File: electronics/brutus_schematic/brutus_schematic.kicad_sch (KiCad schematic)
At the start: 5 parts, among them U1 PCA9685PW, U2 ESP32 DevKit

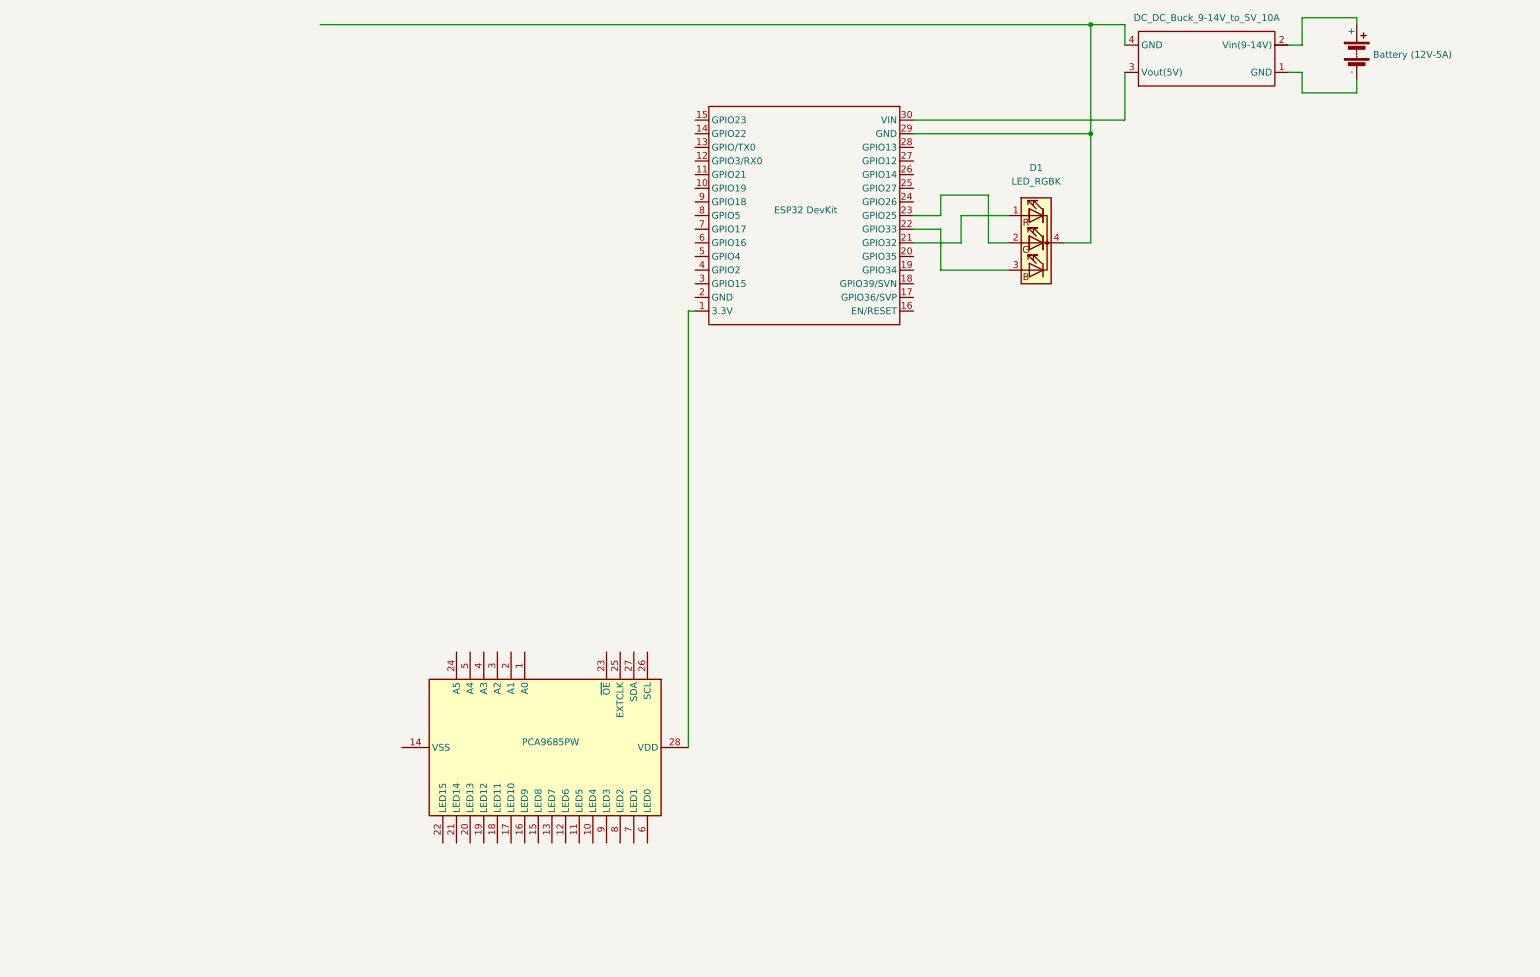
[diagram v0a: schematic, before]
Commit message: Added and connected servos, added and connected ultrasonic sensors, changed LED RGB GND pin
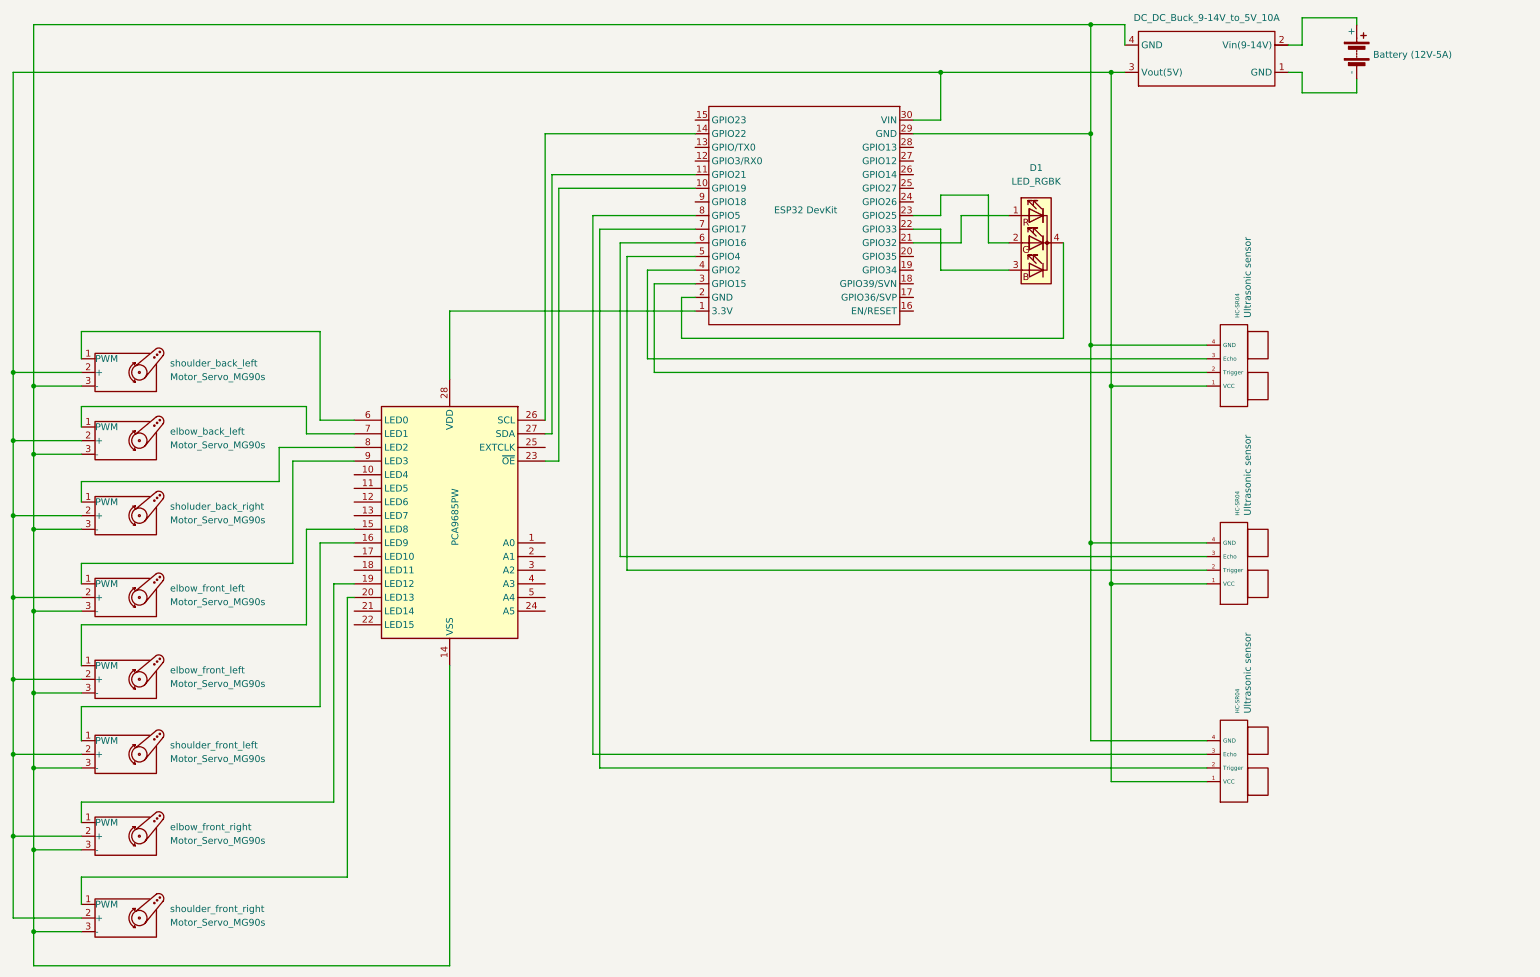
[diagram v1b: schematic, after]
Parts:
- added HC-SR04 (x3): Ultrasonic sensor, symbol hc-sr04:hc-sr04
- added elbow_back_left, elbow_front_left (x2), elbow_front_right, sholuder_back_right, shoulder_back_left, shoulder_front_left, shoulder_front_right: Motor_Servo_MG90s, symbol Motor:Motor_Servo
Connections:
- net at U1.14 (VSS): now also DCB.4 (GND), U2.29 (GND), HC-SR04.4 (GND), HC-SR04.4 (GND), HC-SR04.4 (GND), elbow_back_left.3 (-), elbow_front_left.3 (-), elbow_front_left.3 (-), elbow_front_right.3 (-), sholuder_back_right.3 (-), shoulder_back_left.3 (-), shoulder_front_left.3 (-), shoulder_front_right.3 (-)
- net at U1.15 (LED8): now also elbow_front_left.1 (PWM)
- net at U1.16 (LED9): now also shoulder_front_left.1 (PWM)
- net at U1.19 (LED12): now also elbow_front_right.1 (PWM)
- net at U1.20 (LED13): now also shoulder_front_right.1 (PWM)
- net at U1.23 (~{OE}): now also U2.10 (GPIO19)
- net at U1.26 (SCL): now also U2.14 (GPIO22)
- net at U1.27 (SDA): now also U2.11 (GPIO21)
- net at U1.6 (LED0): now also shoulder_back_left.1 (PWM)
- net at U1.7 (LED1): now also elbow_back_left.1 (PWM)
- net at U1.8 (LED2): now also sholuder_back_right.1 (PWM)
- net at U1.9 (LED3): now also elbow_front_left.1 (PWM)
- net at DCB.3 (Vout(5V)), U2.30 (VIN): now also HC-SR04.1 (VCC), HC-SR04.1 (VCC), HC-SR04.1 (VCC), elbow_back_left.2 (+), elbow_front_left.2 (+), elbow_front_left.2 (+), elbow_front_right.2 (+), sholuder_back_right.2 (+), shoulder_back_left.2 (+), shoulder_front_left.2 (+), shoulder_front_right.2 (+)
- net at U2.2 (GND): now also D1.4 (K)
- net at U2.3 (GPIO15): now also HC-SR04.2 (Trigger)
- net at U2.4 (GPIO2): now also HC-SR04.3 (Echo)
- net at U2.5 (GPIO4): now also HC-SR04.2 (Trigger)
- net at U2.6 (GPIO16): now also HC-SR04.3 (Echo)
- net at U2.7 (GPIO17): now also HC-SR04.2 (Trigger)
- net at U2.8 (GPIO5): now also HC-SR04.3 (Echo)

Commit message: adding switch to kiCad
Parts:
- added SWITCH: SW1, Button_Switch_SMD:Nidec_Copal_CAS-120A, symbol Switch:SW_Nidec_CAS-120A1
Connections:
- net at BT.2 (-): now also SWITCH.2 (B); no longer DCB.1 (GND)
- new net: DCB.1 (GND), SWITCH.3 (A)
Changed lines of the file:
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@@
+	)
+	(junction
+		(at 273.05 27.94)
+		(diameter 0)
+		(color 0 0 0 0)
 	)
 	(junction
@@
 	(wire
 		(pts
-			(xy 254 15.24) (xy 264.16 15.24)
+			(xy 254 15.24) (xy 273.05 15.24)
 		)
 		(stroke
@@
 	(wire
 		(pts
+			(xy 254 25.4) (xy 254 26.67)
+		)
+		(stroke
+			(width 0)
+			(type default)
+		)
+	)
+	(wire
+		(pts
 			(xy 199.39 57.15) (xy 195.58 57.15)
 		)
@@
 	(wire
 		(pts
-			(xy 264.16 26.67) (xy 264.16 29.21)
-		)
-		(stroke
-			(width 0)
-			(type default)
-		)
-	)
-	(wire
-		(pts
 			(xy 218.44 157.48) (xy 218.44 120.65)
 		)
@@
 	(wire
 		(pts
+			(xy 254 26.67) (xy 257.81 26.67)
+		)
+		(stroke
+			(width 0)
+			(type default)
+		)
+	)
+	(wire
+		(pts
 			(xy 17.78 154.94) (xy 26.67 154.94)
 		)
@@
 	(wire
 		(pts
-			(xy 264.16 15.24) (xy 264.16 16.51)
+			(xy 273.05 15.24) (xy 273.05 17.78)
 		)
 		(stroke
@@
 	(wire
 		(pts
-			(xy 254 25.4) (xy 254 29.21)
-		)
-		(stroke
-			(width 0)
-			(type default)
-		)
-	)
-	(wire
-		(pts
 			(xy 121.92 52.07) (xy 140.97 52.07)
 		)
@@
 	(wire
 		(pts
-			(xy 254 29.21) (xy 264.16 29.21)
-		)
-		(stroke
-			(width 0)
-			(type default)
-		)
-	)
-	(wire
-		(pts
 			(xy 114.3 92.71) (xy 114.3 44.45)
 		)
@@
 	(wire
 		(pts
+			(xy 273.05 26.67) (xy 273.05 27.94)
+		)
+		(stroke
+			(width 0)
+			(type default)
+		)
+	)
+	(wire
+		(pts
 			(xy 236.22 115.57) (xy 127 115.57)
 		)
@@
 	(wire
 		(pts
+			(xy 251.46 25.4) (xy 254 25.4)
+		)
+		(stroke
+			(width 0)
+			(type default)
+		)
+	)
+	(wire
+		(pts
 			(xy 26.67 81.28) (xy 13.97 81.28)
 		)
@@
 	(wire
 		(pts
+			(xy 273.05 27.94) (xy 273.05 29.21)
+		)
+		(stroke
+			(width 0)
+			(type default)
+		)
+	)
+	(wire
+		(pts
 			(xy 26.67 161.29) (xy 73.66 161.29)
 		)
@@
 	(wire
 		(pts
-			(xy 254 25.4) (xy 251.46 25.4)
+			(xy 267.97 29.21) (xy 273.05 29.21)
 		)
 		(stroke
@@
 	)
 	(symbol
+		(lib_id "Switch:SW_Nidec_CAS-120A1")
+		(at 262.89 29.21 0)
+		(mirror y)
+		(unit 1)
+		(exclude_from_sim no)
+		(in_bom yes)
+		(on_board yes)
+		(dnp no)
+		(property "Reference" "SWITCH"
+			(at 262.89 21.59 0)
+			(effects
+				(font
+					(size 1.27 1.27)
+				)
+			)
+		)
+		(property "Value" "SW1"
+			(at 262.89 24.13 0)
+			(effects
+				(font
+					(size 1.27 1.27)
+				)
+			)
+		)
+		(property "Footprint" "Button_Switch_SMD:Nidec_Copal_CAS-120A"
+			(at 262.89 39.37 0)
+			(effects
+				(font
+					(size 1.27 1.27)
+				)
+				(hide yes)
+			)
+		)
+		(property "Datasheet" "https://www.nidec-components.com/e/catalog/switch/cas.pdf"
+			(at 262.89 36.83 0)
+			(effects
+				(font
+					(size 1.27 1.27)
+				)
+				(hide yes)
+			)
+		)
+		(property "Description" "Switch, single pole double throw"
+			(at 262.89 29.21 0)
+			(effects
+				(font
+					(size 1.27 1.27)
+				)
+				(hide yes)
+			)
+		)
+		(pin "3"
+		)
+		(pin "1"
+		)
+		(pin "2"
+		)
+		(instances
+			(project ""
+				(path "/157433d3-5d42-4d96-bdf8-aa456a46ad3d"
+					(reference "SWITCH")
+					(unit 1)
+				)
+			)
+		)
+	)
+	(symbol
 		(lib_id "voltage_reduction:DC_DC_Buck_9-14V_to_5V_10A")
 		(at 236.22 22.86 0)
@@
 	(symbol
 		(lib_id "Device:Battery")
-		(at 264.16 21.59 0)
+		(at 273.05 22.86 0)
 		(unit 1)
 		(exclude_from_sim no)
@@
 		(dnp no)
 		(property "Reference" "BT"
-			(at 267.97 19.7484 0)
+			(at 276.86 21.0184 0)
 			(effects
 				(font
@@
 		)
 		(property "Value" "Battery (12V-5A)"
-			(at 267.208 22.098 0)
+			(at 276.098 23.368 0)
 			(effects
 				(font
@@
 		)
 		(property "Footprint" ""
-			(at 264.16 20.066 90)
+			(at 273.05 21.336 90)
 			(effects
 				(font
@@
 		)
 		(property "Datasheet" "~"
-			(at 264.16 20.066 90)
+			(at 273.05 21.336 90)
 			(effects
 				(font
@@
 		)
 		(property "Description" "Multiple-cell battery"
-			(at 264.16 21.59 0)
-			(effects
-				(font
+			(at 273.05 22.86 0)
+			(effects
+				(font
